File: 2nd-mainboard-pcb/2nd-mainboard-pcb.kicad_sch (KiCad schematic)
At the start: 19 parts, among them J1 USB_C_Receptacle, J16 Power, SW1 SW_DIP_x01, U2 FT232RL

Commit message: verpolungsschutz und powerin
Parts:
- removed C1, C2: 100nF, symbol Device:C
- removed C13: 0.1µF, Capacitor_SMD:CP_Elec_5x3, symbol Device:C_Polarized
- removed C4: 1uF, symbol Device:C
- removed D1: SMAJ5.0A, Diode_SMD:D_SMA, symbol Diode:SMAJ5.0A
- removed D2: LED, symbol Device:LED
- removed J1: USB_C_Receptacle, Connector_USB:USB_C_Receptacle_GCT_USB4085, symbol Connector:USB_C_Receptacle
- removed JP2: MEASO, Jumper:SolderJumper-2_P1.3mm_Bridged_Pad1.0x1.5mm, symbol Jumper:SolderJumper_2_Bridged
- removed R2, R3: 5k1, symbol Device:R
- removed R4, R5: 10k, symbol Device:R
- removed SW1: SW_DIP_x01, Button_Switch_SMD:SW_SPST_EVQQ2, symbol Switch:SW_DIP_x01
- removed U2: FT232RL, Package_SO:SSOP-28_5.3x10.2mm_P0.65mm, symbol Interface_USB:FT232RL
- added C13, C14, C8: 10µF, symbol Device:C
- added C16: 22nF, symbol Device:C
- added D8: WE-TVSP_DO-214AA_600W_BI, WE-TVSP_DO-214AA_600W_BI:WE-TVSP_DO-214AA_BIDIRECTIONAL, symbol Imported_Component_Symbols:WE-TVSP_DO-214AA_600W_BI
- added R20: 100k, symbol Device:R
- added U6: SQJ409EP-T1_GE3, Imported_Component_Footprints:SQJ409EP_T1_GE3, symbol Imported_Component_Symbols:SQJ409EP-T1_GE3
- added U7: SZ1SMB5927BT3G, Imported_Component_Footprints:SZ1SMB5927BT3G, symbol Imported_Component_Symbols:SZ1SMB5927BT3G
- added U8: TPS565208, Package_TO_SOT_SMD:SOT-23-6, symbol Regulator_Switching:TPS565208
- added U9: TPS56837HRPAR, Imported_Component_Footprints:TPS56837HRPAR, symbol Imported_Component_Symbols:TPS56837HRPAR
- C15: value 0.22µF -> 100nF; footprint Capacitor_SMD:C_0402_1005Metric -> (none)
- C17: value 0.1µF -> 100nF; footprint Capacitor_SMD:C_0402_1005Metric -> (none)
- R1: value 10k -> 30.1k
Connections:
- net RESET is gone; now on net GND: R1.2
- net +12V: now also J16.1 (Pin_1), D8.2, U6.5 (D); no longer C15.1, C17.1
- net GND: now also C13.2, C14.2, C16.2, C8.2; no longer C17.2
- net GND2: now also D8.1, R20.2
- net +5V: no longer names the net of R1.1
- net +5V: now also U9.10 (MODE)
- new net: R20.1, U6.4 (G), U7.2 (A)
- new net: C16.1, U9.5 (SS)
- new net: C17.1, U9.7 (BOOT)
- new net PWR_IN_PROT: C13.1, C14.1, C15.1, C8.1, U6.1, U6.2, U6.3 (S), U7.1 (K), U9.8 (VIN)
- no-connect marks 21 -> 0
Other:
- added sheet USB-C Eingang (usbc.kicad_sch)
- note added: "Da der 3D Drucker nicht immer verlässlich 24V Versorgungsspannung gibt, wird hier ein Buck Converter verbaut um mögliche 24V auf 12V herunterzuregeln, um die Fans nicht zu schädigen"
- note added: "Leistungs-Eingang 24V"
- note added: "Spannungswandler auf 12V"
- note added: "Spannungswandler auf 5V"
- note added: "Verpolungsschutzschaltung Und Schutz vor Überspannung mit TSV Diode"
- note removed: "Da der 3D Drucker nicht immer verlässlich 24V Versorgungsspannung gibt, kann hier ein LM2596 verbaut werden um mögliche 24V auf 12V herunterzuregeln, um die Fans nicht zu schädigne"
- note removed: "Leistungs-Eingang 12V/5V"
- moved on the sheet: J16, R18

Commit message: finished stacked design, annotaded
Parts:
- removed C14: 10µF, symbol Device:C
- removed C15, C17: 100nF, symbol Device:C
- removed C16: 22nF, symbol Device:C
- removed R1: 30.1k, symbol Device:R
- removed U9: TPS56837HRPAR, Imported_Component_Footprints:TPS56837HRPAR, symbol Imported_Component_Symbols:TPS56837HRPAR
- added C1, C2, C3, C4, C5: 10µF, symbol Device:C
- added C10, C6, C9: 100nF, symbol Device:C
- added C11, C7: 22nF, symbol Device:C
- added C12: 22µF, symbol Device:C
- added L1: 4.7µH, symbol Device:L
- added L2: 3.3µH, symbol Device:L
- added R3: 30.1k, symbol Device:R
- added R4: 100k, symbol Device:R
- added R5: 54.9k, symbol Device:R
- added R6: 10k, symbol Device:R
- added R7: 30k, symbol Device:R
- added R8: 1k58, symbol Device:R
- added U3: TPS56837HRPAR, Imported_Component_Footprints:TPS56837HRPAR, symbol Imported_Component_Symbols:TPS56837HRPAR
- C13: value 10µF -> 47µF
- C8: value 10µF -> 100nF
- renumbered D8 to D1, J16 to J1, R18 to R1, R20 to R2, U6 to U1, U7 to U2, U8 to U4
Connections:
- net +12V: now also C13.1, C8.1, U4.3 (VIN), U4.5 (EN), C11.1, C3.1, C5.1, L1.2, R7.1; no longer D1.2, J1.1 (Pin_1), U1.5 (D)
- net GND: now also U4.1 (GND), C1.2, C12.2, C2.2, C3.2, C4.2, C5.2, C6.2, C7.2, R3.2, R6.2, R8.2, U3.3 (AGND), U3.9 (PGND)
- net PWR_IN_PROT: now also C1.1, C2.1, C4.1, C6.1, U3.8 (VIN); no longer C13.1, C8.1
- net at U4.2 (SW): now also C10.2, L2.1
- net at U4.4 (VFB): now also R5.2, R6.1
- net at U4.6 (VBST): now also C10.1
- new net: R3.1, U3.10 (MODE)
- new net: C11.2, R7.2, R8.1, U3.2 (FB)
- new net: R4.2, U3.4 (PG)
- new net: C7.1, U3.5 (SS)
- new net: C9.2, L1.1, U3.6 (SW)
- new net: C9.1, U3.7 (BOOT)
- new net +24V: D1.2, J1.1 (Pin_1), U1.5 (D)
- new net +5V_POW: C12.1, L2.2, R5.1
- new net +5V_USBC: R4.1
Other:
- note added: "Für den Betrieb des Wandlers werden stabile 5 V benötigt, um die internen Logikblöcke und Gate-Treiber zu versorgen und die Verlustleistung zu reduzieren. Diese Versorgung kann vom USB‑C‑Eingang stammen, der in der Regel ausreichend Strom (mindestens 500 mA) bereitstellt und durch geeignete Filter- und Entstörmaßnahmen stabilisiert werden sollte."
- note added: "Leistungs-Eingang 3D-Drucker Netzteil Kann entweder 24 od. 12V sein"
- note added: "TSV-Diode als überspannugnsschutz bei zB Kontakt mit aufgeladenem Mensch"
- note added: "Zener Diode hat folgenden Effekt: Die durchbruchspannung ist stabil und somit kann Vgs nicht überlastet werden"
- note removed: "Leistungs-Eingang 24V"
- moved on the sheet: D1, R1, R2, U1, U2, U4

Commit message: alle bauteile hinzugefügt
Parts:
- removed J1: Power, symbol Connector:Conn_01x02_Pin
- added C7: 100nF, Capacitor_SMD:C_0402_1005Metric_Pad0.74x0.62mm_HandSolder, symbol Device:C
- added J1: PJ-082BH, Imported_Component_Footprints:CUI_PJ-082BH, symbol Imported_Component_Symbols:PJ-082BH
- C1: renamed from C9; footprint (none) -> Capacitor_SMD:C_0402_1005Metric_Pad0.74x0.62mm_HandSolder
- C10, C6: footprint (none) -> Capacitor_SMD:C_0402_1005Metric_Pad0.74x0.62mm_HandSolder
- C11: renamed from C3; footprint (none) -> Capacitor_SMD:C_0805_2012Metric_Pad1.18x1.45mm_HandSolder
- C12: renamed from C5; footprint (none) -> Capacitor_SMD:C_0805_2012Metric_Pad1.18x1.45mm_HandSolder
- C13: renamed from C8; footprint (none) -> Capacitor_SMD:C_0402_1005Metric_Pad0.74x0.62mm_HandSolder
- C14: renamed from C12; footprint (none) -> Capacitor_SMD:C_1210_3225Metric_Pad1.33x2.70mm_HandSolder
- C2: renamed from C11; footprint (none) -> Capacitor_SMD:C_1210_3225Metric_Pad1.33x2.70mm_HandSolder
- C3: renamed from C1; footprint (none) -> Capacitor_SMD:C_0805_2012Metric_Pad1.18x1.45mm_HandSolder
- C4: renamed from C2; footprint (none) -> Capacitor_SMD:C_0805_2012Metric_Pad1.18x1.45mm_HandSolder
- C5: renamed from C4; footprint (none) -> Capacitor_SMD:C_1210_3225Metric_Pad1.33x2.70mm_HandSolder
- C8: renamed from C13; footprint (none) -> Capacitor_SMD:C_1210_3225Metric_Pad1.33x2.70mm_HandSolder
- C9: renamed from C7; footprint (none) -> Capacitor_SMD:C_1210_3225Metric_Pad1.33x2.70mm_HandSolder
- D1: footprint WE-TVSP_DO-214AA_600W_BI:WE-TVSP_DO-214AA_BIDIRECTIONAL -> Imported_Component_Footprints:824521241
- L1: footprint (none) -> Imported_Component_Footprints:SPM10040T_4R7M_HZ
- L2: footprint (none) -> Imported_Component_Footprints:IHLP2525CZER3R3M11
- R1: renamed from R2; footprint (none) -> Resistor_SMD:R_0402_1005Metric
- R2: renamed from R4; footprint (none) -> Resistor_SMD:R_0402_1005Metric
- R3: renamed from R7; footprint (none) -> Resistor_SMD:R_0402_1005Metric
- R4: renamed from R8; footprint (none) -> Resistor_SMD:R_0402_1005Metric
- R5: renamed from R3; footprint (none) -> Resistor_SMD:R_0402_1005Metric
- R6: renamed from R1; footprint (none) -> Resistor_SMD:R_0402_1005Metric
- R7: renamed from R5; footprint (none) -> Resistor_SMD:R_0402_1005Metric
- R8: renamed from R6; footprint (none) -> Resistor_SMD:R_0402_1005Metric
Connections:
- net +24V: now also J1.1
- net GND2: now also C7.2, J1.2
- new net GND3: C7.1, J1.SH1 (SHIELD), J1.SH2 (SHIELD__1), J1.SH3 (SHIELD__2), J1.SH4 (SHIELD__3)
- no-connect marks 0 -> 1
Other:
- note added: "Noise-Reduction"
- moved on the sheet: D1, R1, R6, U1, U2

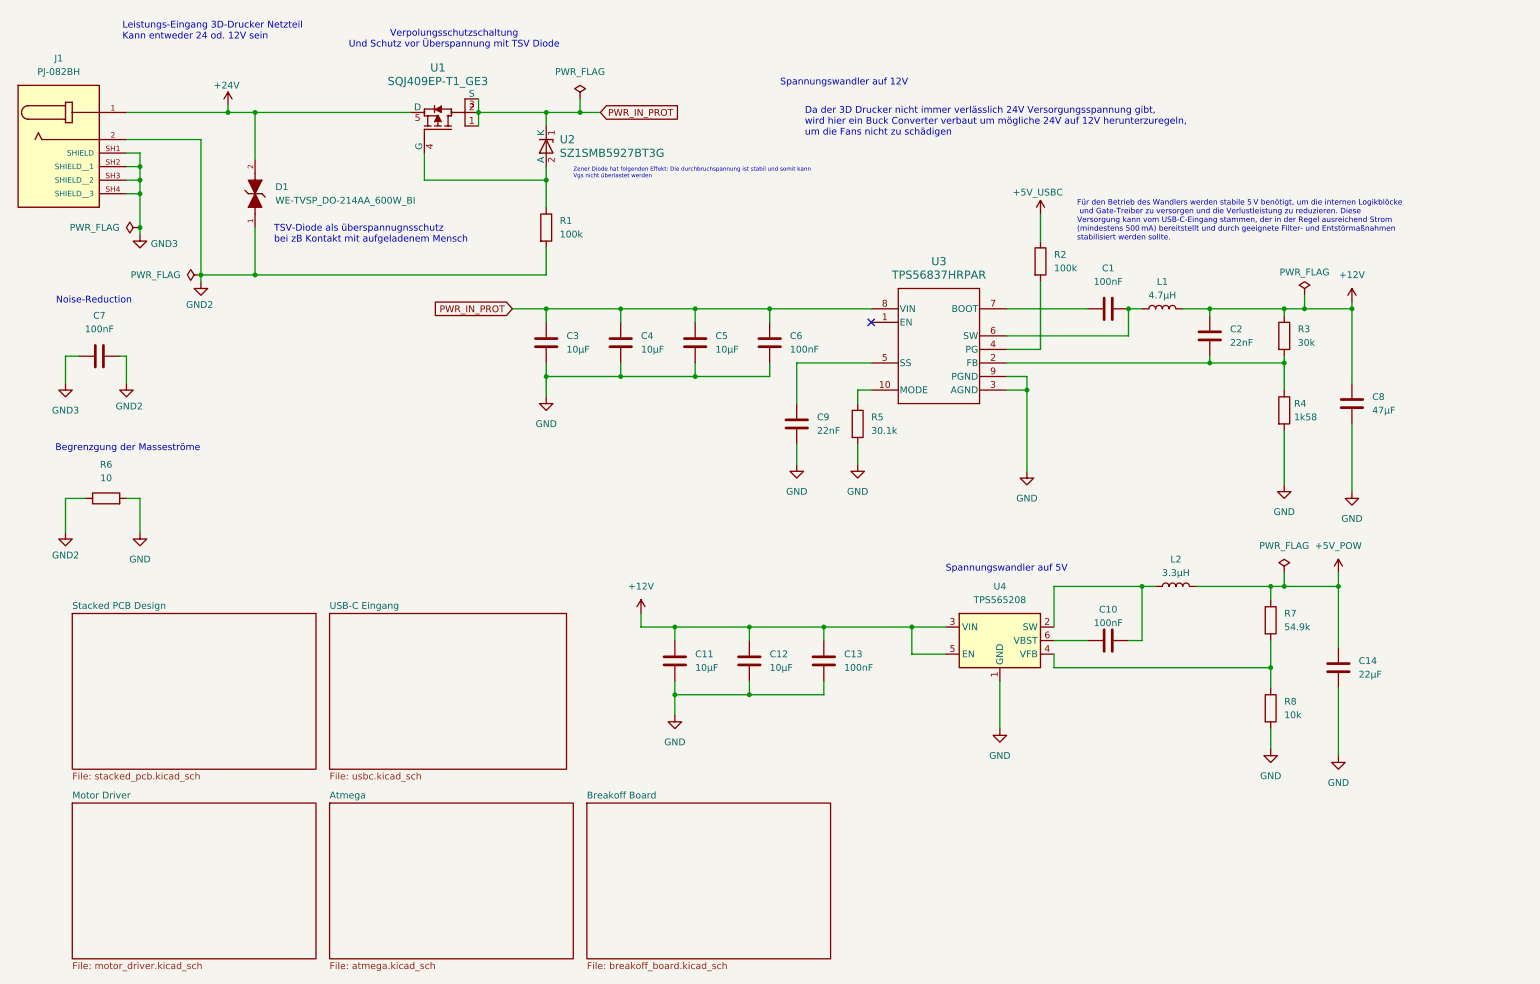
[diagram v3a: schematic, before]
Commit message: updated a bit of the track widths, removed comments in schematic
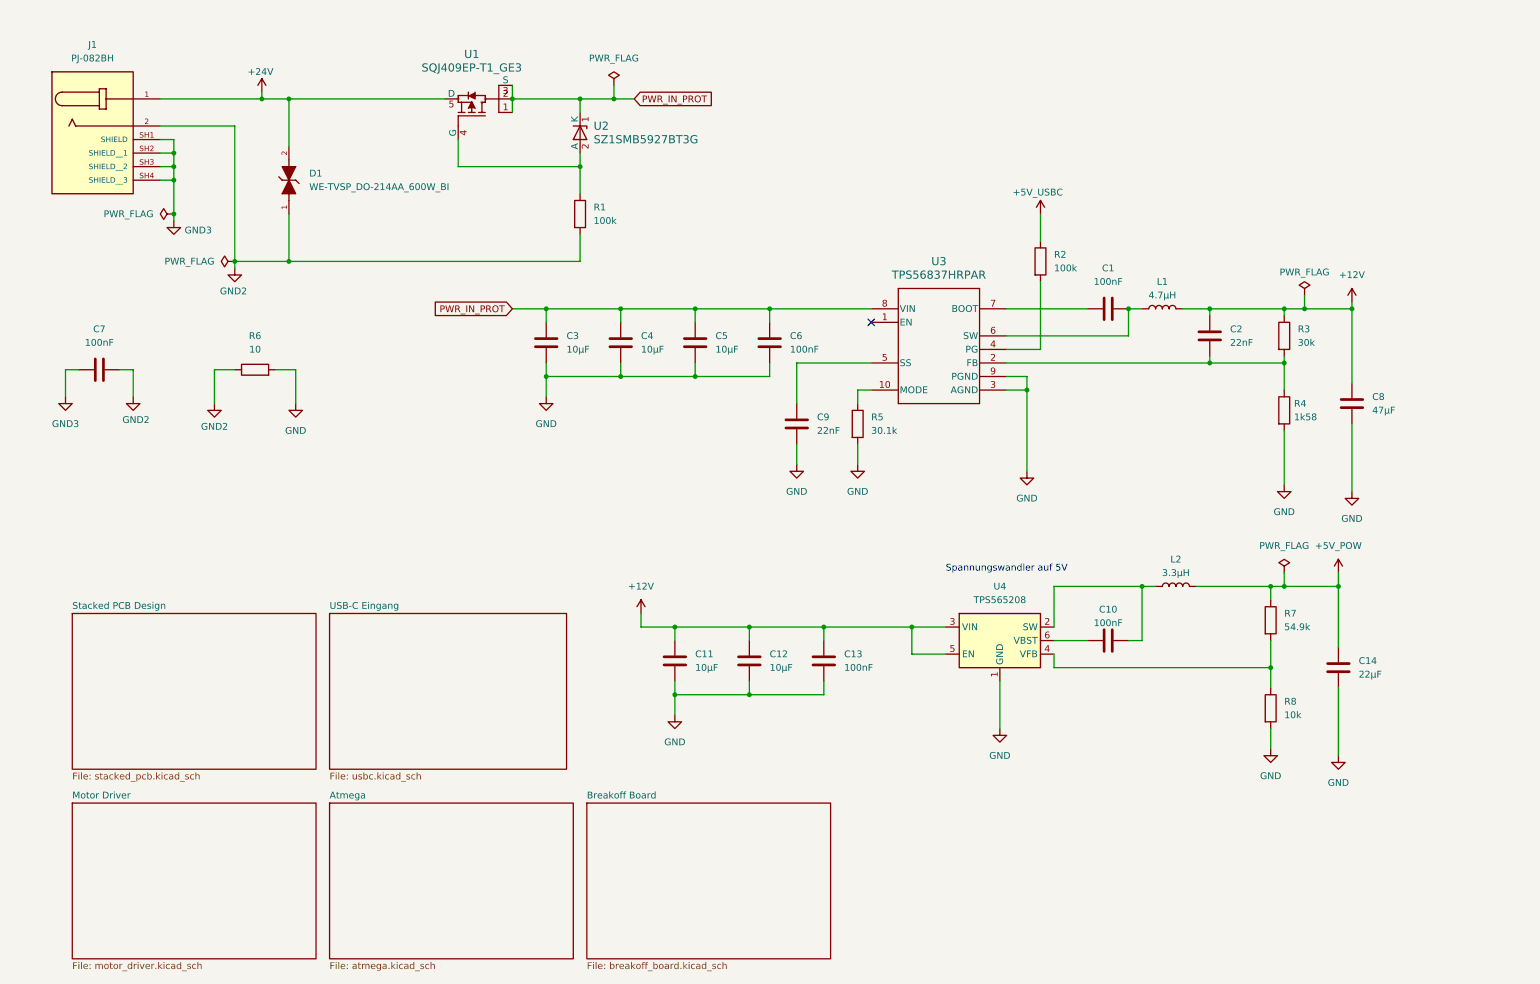
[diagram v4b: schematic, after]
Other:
- note removed: "Begrenzgung der Masseströme"
- note removed: "Da der 3D Drucker nicht immer verlässlich 24V Versorgungsspannung gibt, wird hier ein Buck Converter verbaut um mögliche 24V auf 12V herunterzuregeln, um die Fans nicht zu schädigen"
- note removed: "Für den Betrieb des Wandlers werden stabile 5 V benötigt, um die internen Logikblöcke und Gate-Treiber zu versorgen und die Verlustleistung zu reduzieren. Diese Versorgung kann vom USB‑C‑Eingang stammen, der in der Regel ausreichend Strom (mindestens 500 mA) bereitstellt und durch geeignete Filter- und Entstörmaßnahmen stabilisiert werden sollte."
- note removed: "Leistungs-Eingang 3D-Drucker Netzteil Kann entweder 24 od. 12V sein"
- note removed: "Noise-Reduction"
- note removed: "Spannungswandler auf 12V"
- note removed: "TSV-Diode als überspannugnsschutz bei zB Kontakt mit aufgeladenem Mensch"
- note removed: "Verpolungsschutzschaltung Und Schutz vor Überspannung mit TSV Diode"
- note removed: "Zener Diode hat folgenden Effekt: Die durchbruchspannung ist stabil und somit kann Vgs nicht überlastet werden"
- moved on the sheet: C7, D1, J1, R1, R6, U1, U2

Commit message: noch mehr bauteile ausgetauscht
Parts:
- R2: footprint Resistor_SMD:R_0402_1005Metric -> Resistor_SMD:R_0603_1608Metric
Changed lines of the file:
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@@
 			)
 		)
-		(property "Footprint" "Resistor_SMD:R_0402_1005Metric"
+		(property "Footprint" "Resistor_SMD:R_0603_1608Metric"
 			(at 203.962 59.69 90)
 			(effects

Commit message: stacked pcb reworked
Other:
- note removed: "Spannungswandler auf 5V"
- moved on the sheet: C1, C10, C11, C12, C13, C14, C2, C3, C4, C5, C6, C7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
